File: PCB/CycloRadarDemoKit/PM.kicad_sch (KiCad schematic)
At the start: 47 parts, among them J401 20-16V Supply Voltage, Q401 SI2309CDS, U401 INA3221, U402 RT8259, U403 TPS2121RUXR, U404 AP63205WU, U405 AP63203WU

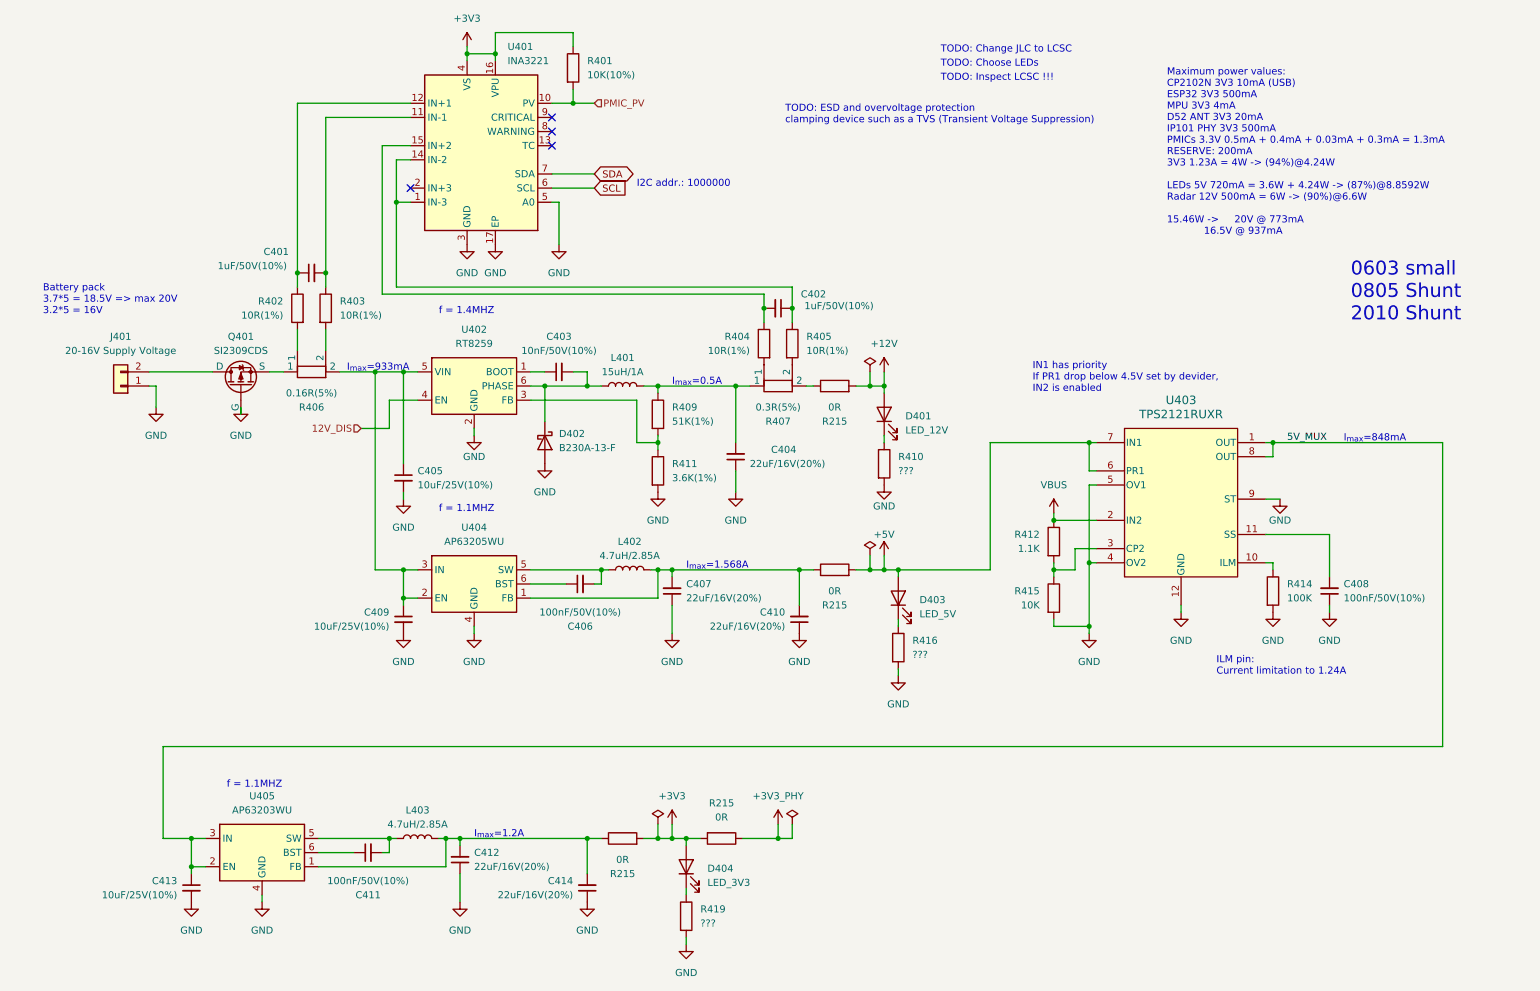
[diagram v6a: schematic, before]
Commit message: MPU added, power managemennt updated
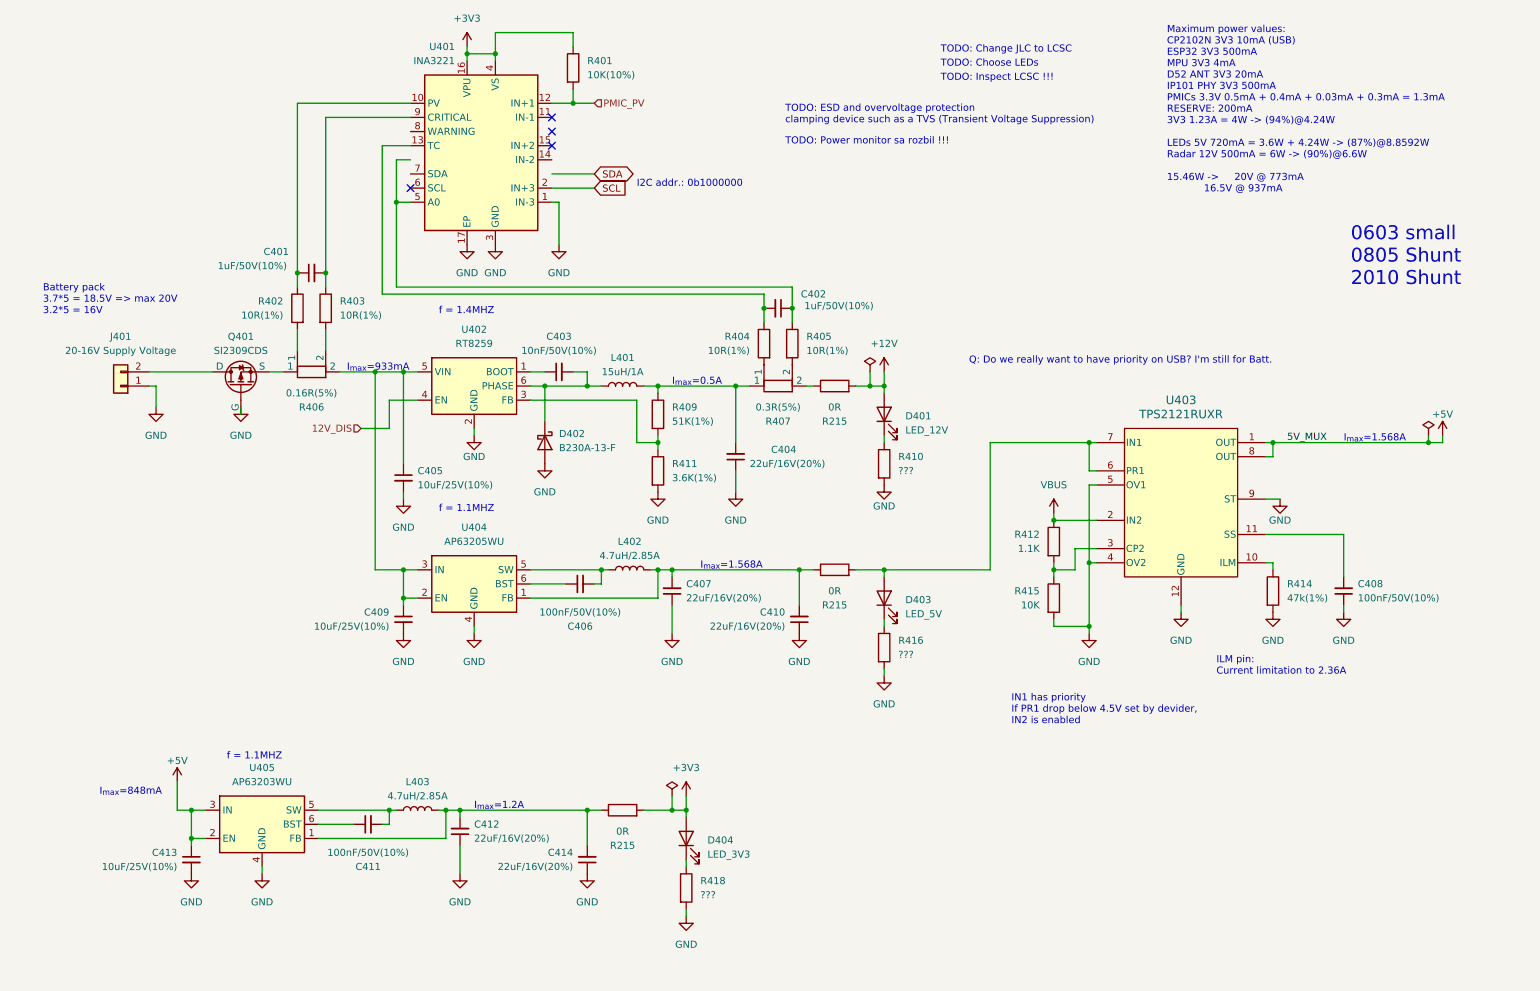
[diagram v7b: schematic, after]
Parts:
- removed R215: 0R, Resistor_SMD:R_0805_2012Metric, symbol Device:R
- R414: value 100K -> 47k(1%); footprint (none) -> Resistor_SMD:R_0603_1608Metric; LCSC (none) -> 0603
- renumbered R419 to R418
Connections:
- net 5V_MUX is gone; now on net +5V: C413.1, U403.1 (OUT), U403.8 (OUT), U405.2 (EN), U405.3 (IN)
- net +5V: no longer D403.2 (A), R215.2, U403.6 (PR1), U403.7 (IN1)
- net GND: now also U401.1 (IN-3); no longer U401.5 (A0)
- net PMIC_PV: now also U401.12 (IN+1); no longer U401.10 (PV)
- net SCL: now also U401.2 (IN+3); no longer U401.6 (SCL)
- net SDA: no longer U401.7 (SDA)
- net at C402.1, R405.1: now also U401.5 (A0); no longer U401.1 (IN-3), U401.14 (IN-2)
- net at C401.2, R403.1: now also U401.9 (CRITICAL); no longer U401.11 (IN-1)
- net at C401.1, R402.1: now also U401.10 (PV); no longer U401.12 (IN+1)
- net at U401.13 (TC): now also C402.2, R404.1
- new net: D403.2 (A), R215.2, U403.6 (PR1), U403.7 (IN1)
- now unconnected: U401.15 (IN+2)
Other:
- note added: "I2C addr.: 0b1000000"
- note added: "ILM pin: Current limitation to 2.36A"
- note added: "Q: Do we really want to have priority on USB? I'm still for Batt."
- note added: "TODO: Power monitor sa rozbil !!!"
- note removed: "I2C addr.: 1000000"
- note removed: "ILM pin: Current limitation to 1.24A"
- moved on the sheet: C408, C411, C412, C413, C414, D403, D404, L403, R215, R416, R418, U405

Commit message: added buzzer and pins for Radar
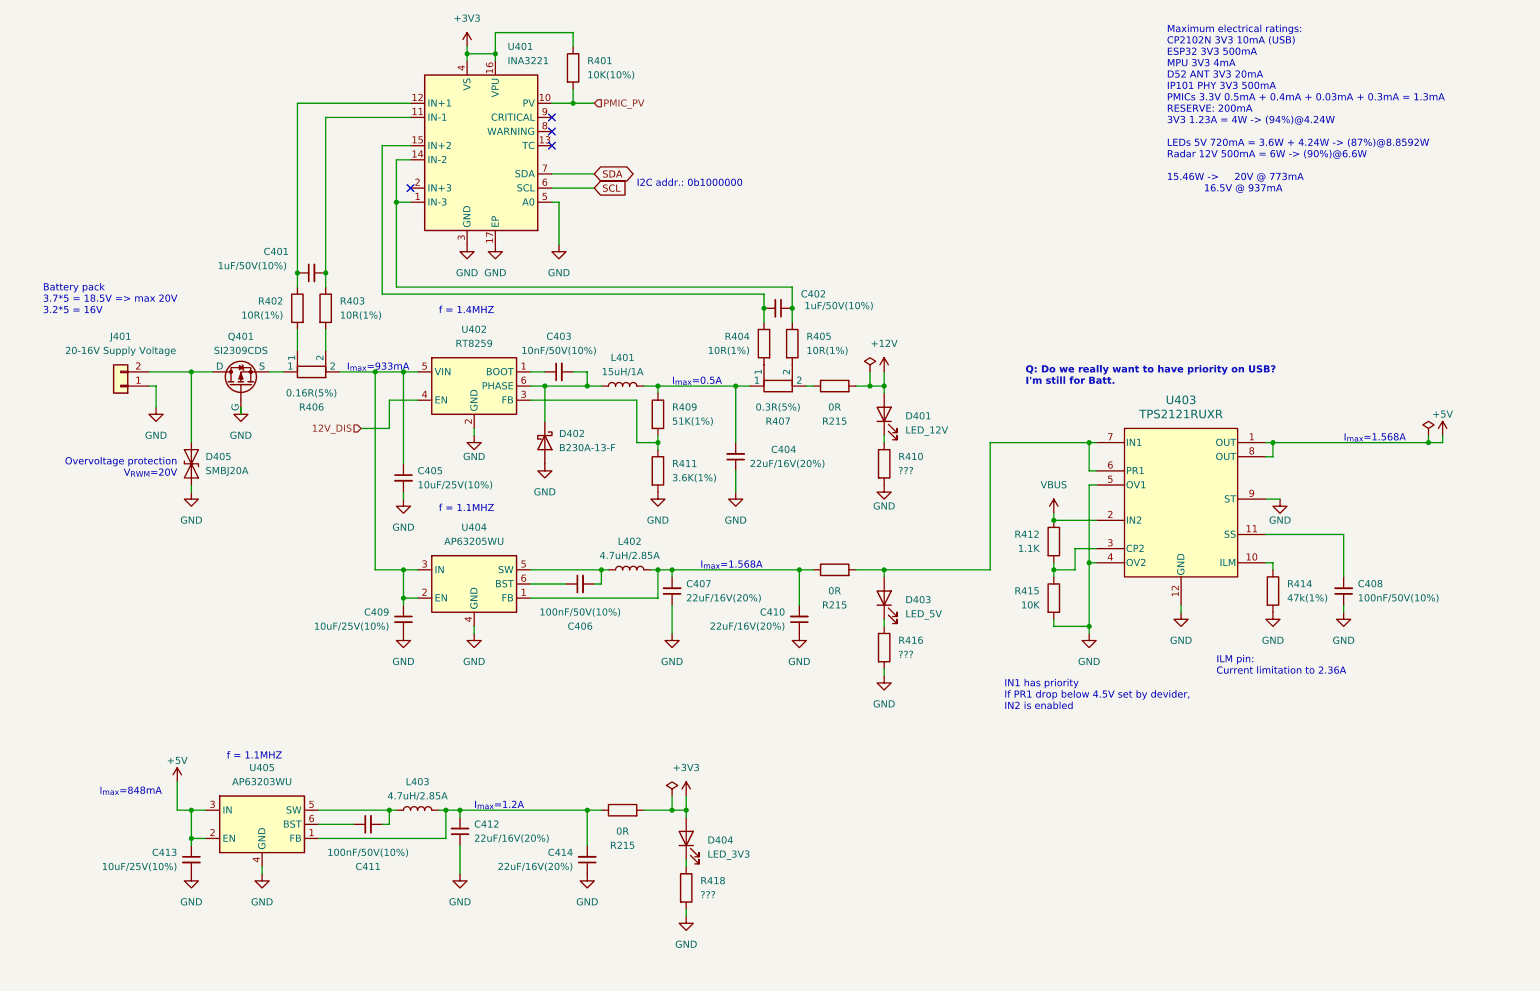
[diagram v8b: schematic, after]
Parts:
- added D405: SMBJ20A, Diode_SMD:D_SMB, symbol Diode:SD05_SOD323
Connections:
- net GND: now also U401.5 (A0), D405.1 (A1); no longer U401.1 (IN-3)
- net PMIC_PV: now also U401.10 (PV); no longer U401.12 (IN+1)
- net SCL: now also U401.6 (SCL); no longer U401.2 (IN+3)
- net SDA: now also U401.7 (SDA)
- net at C401.1, R402.1: now also U401.12 (IN+1); no longer U401.10 (PV)
- net at U401.11 (IN-1): now also C401.2, R403.1
- net at C402.2, R404.1: now also U401.15 (IN+2); no longer U401.13 (TC)
- net at U401.14 (IN-2): now also C402.1, R405.1, U401.1 (IN-3)
- net at J401.2 (Pin_2), Q401.1 (D): now also D405.2 (A2)
- now unconnected: U401.9 (CRITICAL)
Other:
- note added: "Maximum electrical ratings: CP2102N 3V3 10mA (USB) ESP32 3V3 500mA MPU 3V3 4mA D52 ANT 3V3 20mA IP101 PHY 3V3 500mA PMICs 3.3V 0.5mA + 0.4mA + 0.03mA + 0.3mA = 1.3mA RESERVE: 200mA 3V3 1.23A = 4W -> (94%)@4.24W LEDs 5V 720mA = 3.6W + 4.24W -> (87%)@8.8592W Radar 12V 500mA = 6W -> (90%)@6.6W 15.46W -> 20V @ 773mA 16.5V @ 937mA"
- note added: "Overvoltage protection V_{RWM}=20V"
- note removed: "0603 small 0805 Shunt 2010 Shunt"
- note removed: "Maximum power values: CP2102N 3V3 10mA (USB) ESP32 3V3 500mA MPU 3V3 4mA D52 ANT 3V3 20mA IP101 PHY 3V3 500mA PMICs 3.3V 0.5mA + 0.4mA + 0.03mA + 0.3mA = 1.3mA RESERVE: 200mA 3V3 1.23A = 4W -> (94%)@4.24W LEDs 5V 720mA = 3.6W + 4.24W -> (87%)@8.8592W Radar 12V 500mA = 6W -> (90%)@6.6W 15.46W -> 20V @ 773mA 16.5V @ 937mA"
- note removed: "TODO: Change JLC to LCSC"
- note removed: "TODO: Choose LEDs"
- note removed: "TODO: ESD and overvoltage protection clamping device such as a TVS (Transient Voltage Suppression)"
- note removed: "TODO: Inspect LCSC !!!"
- note removed: "TODO: Power monitor sa rozbil !!!"
